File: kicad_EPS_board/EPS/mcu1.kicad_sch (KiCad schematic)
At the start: 37 parts, among them J10 UEXT, P6 CONN_01X02, U10 W25Q80DVS, U11 STM32G431CBTx, Y2 8MHz

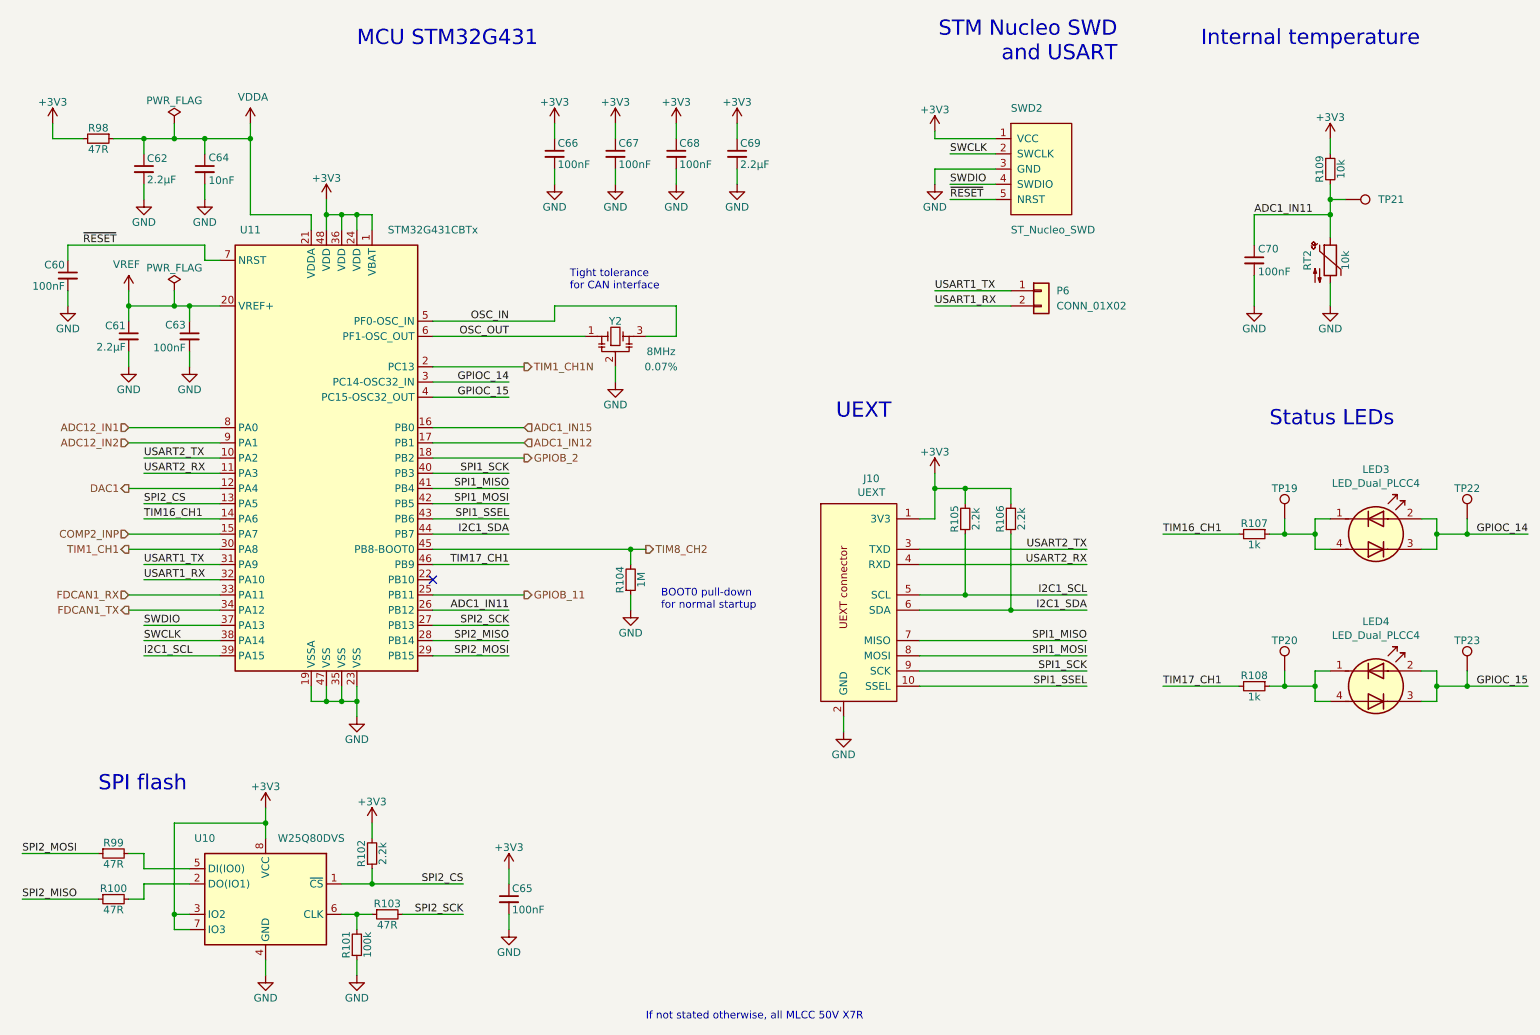
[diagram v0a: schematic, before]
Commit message: kicad EPS board V2 revision and already generated html doc files
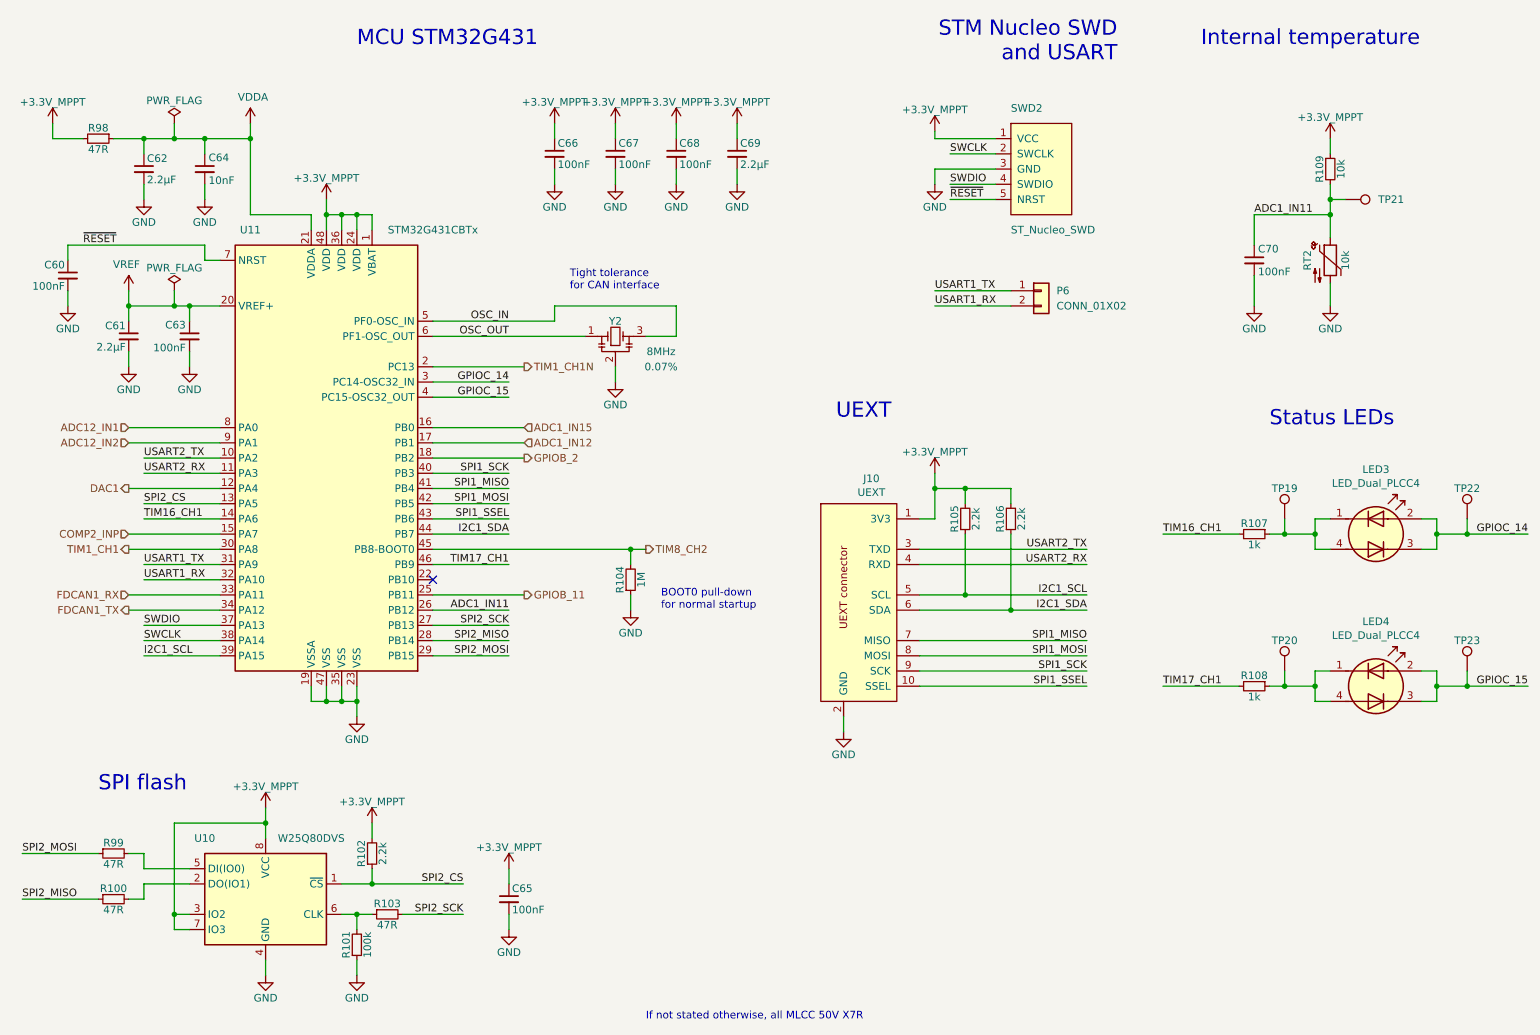
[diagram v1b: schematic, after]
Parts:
- RT2: footprint Capacitor_THT:C_Disc_D3.8mm_W2.6mm_P2.50mm -> Resistor_SMD:R_0603_1608Metric
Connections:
- net +3V3 renamed +3.3V_MPPT
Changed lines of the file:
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@@
 (kicad_sch
-	(version 20231120)
+	(version 20250114)
 	(generator "eeschema")
-	(generator_version "8.0")
+	(generator_version "9.0")
 	(paper "A4")
+	(text "MCU STM32G431"
+		(exclude_from_sim no)
+		(at 83.82 21.59 0)
+		(effects
+			(font
+				(size 2.54 2.54)
+			)
+			(justify left bottom)
+		)
+	)
+	(text "SPI flash"
+		(exclude_from_sim no)
+		(at 40.64 146.05 0)
+		(effects
+			(font
+				(size 2.54 2.54)
+			)
+			(justify left bottom)
+		)
+	)
+	(text "If not stated otherwise, all MLCC 50V X7R"
+		(exclude_from_sim no)
+		(at 132.08 184.15 0)
+		(effects
+			(font
+				(size 1.27 1.27)
+			)
+			(justify left bottom)
+		)
+	)
+	(text "Status LEDs"
+		(exclude_from_sim no)
+		(at 236.22 85.09 0)
+		(effects
+			(font
+				(size 2.54 2.54)
+			)
+			(justify left bottom)
+		)
+	)
+	(text "Internal temperature"
+		(exclude_from_sim no)
+		(at 224.79 21.59 0)
+		(effects
+			(font
+				(size 2.54 2.54)
+			)
+			(justify left bottom)
+		)
+	)
+	(text "Tight tolerance\nfor CAN interface"
+		(exclude_from_sim no)
+		(at 119.38 62.23 0)
+		(effects
+			(font
+				(size 1.27 1.27)
+			)
+			(justify left bottom)
+		)
+	)
+	(text "BOOT0 pull-down\nfor normal startup"
+		(exclude_from_sim no)
+		(at 134.62 115.57 0)
+		(effects
+			(font
+				(size 1.27 1.27)
+			)
+			(justify left bottom)
+		)
+	)
+	(text "UEXT"
+		(exclude_from_sim no)
+		(at 163.83 83.82 0)
+		(effects
+			(font
+				(size 2.54 2.54)
+			)
+			(justify left bottom)
+		)
+	)
+	(text "STM Nucleo SWD\nand USART"
+		(exclude_from_sim no)
+		(at 210.82 24.13 0)
+		(effects
+			(font
+				(size 2.54 2.54)
+			)
+			(justify right bottom)
+		)
+	)
 	(junction
 		(at 246.38 49.53)
@@
 		)
 	)
-	(text "MCU STM32G431"
-		(exclude_from_sim no)
-		(at 83.82 21.59 0)
-		(effects
-			(font
-				(size 2.54 2.54)
-			)
-			(justify left bottom)
-		)
-	)
-	(text "SPI flash"
-		(exclude_from_sim no)
-		(at 40.64 146.05 0)
-		(effects
-			(font
-				(size 2.54 2.54)
-			)
-			(justify left bottom)
-		)
-	)
-	(text "If not stated otherwise, all MLCC 50V X7R"
-		(exclude_from_sim no)
-		(at 132.08 184.15 0)
-		(effects
-			(font
-				(size 1.27 1.27)
-			)
-			(justify left bottom)
-		)
-	)
-	(text "Status LEDs"
-		(exclude_from_sim no)
-		(at 236.22 85.09 0)
-		(effects
-			(font
-				(size 2.54 2.54)
-			)
-			(justify left bottom)
-		)
-	)
-	(text "Internal temperature"
-		(exclude_from_sim no)
-		(at 224.79 21.59 0)
-		(effects
-			(font
-				(size 2.54 2.54)
-			)
-			(justify left bottom)
-		)
-	)
-	(text "Tight tolerance\nfor CAN interface"
-		(exclude_from_sim no)
-		(at 119.38 62.23 0)
-		(effects
-			(font
-				(size 1.27 1.27)
-			)
-			(justify left bottom)
-		)
-	)
-	(text "BOOT0 pull-down\nfor normal startup"
-		(exclude_from_sim no)
-		(at 134.62 115.57 0)
-		(effects
-			(font
-				(size 1.27 1.27)
-			)
-			(justify left bottom)
-		)
-	)
-	(text "UEXT"
-		(exclude_from_sim no)
-		(at 163.83 83.82 0)
-		(effects
-			(font
-				(size 2.54 2.54)
-			)
-			(justify left bottom)
-		)
-	)
-	(text "STM Nucleo SWD\nand USART"
-		(exclude_from_sim no)
-		(at 210.82 24.13 0)
-		(effects
-			(font
-				(size 2.54 2.54)
-			)
-			(justify right bottom)
-		)
-	)
 	(label "SPI1_MOSI"
 		(at 109.22 97.79 180)
@@
 			)
 		)
-		(property "Value" "+3V3"
+		(property "Value" "+3.3V_MPPT"
 			(at 68.58 145.034 0)
 			(effects
@@
 			)
 		)
-		(property "Value" "+3V3"
+		(property "Value" "+3.3V_MPPT"
 			(at 86.36 147.574 0)
 			(effects
@@
 			)
 		)
-		(property "Value" "+3V3"
+		(property "Value" "+3.3V_MPPT"
 			(at 180.34 32.004 0)
 			(effects
@@
 			)
 		)
-		(property "Footprint" "Capacitor_THT:C_Disc_D3.8mm_W2.6mm_P2.50mm"
+		(property "Footprint" "Resistor_SMD:R_0603_1608Metric"
 			(at 246.38 55.88 0)
 			(effects
@@
 			)
 		)
-		(property "Value" "+3V3"
+		(property "Value" "+3.3V_MPPT"
 			(at 137.16 30.734 0)
 			(effects
@@
 			)
 		)
-		(property "Value" "+3V3"
+		(property "Value" "+3.3V_MPPT"
 			(at 78.74 43.434 0)
 			(effects
@@
 			)
 		)
-		(property "Value" "+3V3"
+		(property "Value" "+3.3V_MPPT"
 			(at 246.38 33.274 0)
 			(effects
@@
 			)
 		)
-		(property "Value" "+3V3"
+		(property "Value" "+3.3V_MPPT"
 			(at 127 30.734 0)
 			(effects
@@
 			)
 		)
-		(property "Value" "+3V3"
+		(property "Value" "+3.3V_MPPT"
 			(at 180.34 89.154 0)
 			(effects
@@
 			)
 		)
-		(property "Value" "+3V3"
+		(property "Value" "+3.3V_MPPT"
 			(at 147.32 30.734 0)
 			(effects
@@
 			)
 		)
-		(property "Value" "+3V3"
+		(property "Value" "+3.3V_MPPT"
 			(at 116.84 30.734 0)
 			(effects
@@
 			)
 		)
-		(property "Value" "+3V3"
+		(property "Value" "+3.3V_MPPT"
 			(at 33.02 30.734 0)
 			(effects
@@
 			)
 		)
-		(property "Value" "+3V3"
+		(property "Value" "+3.3V_MPPT"
 			(at 109.22 155.194 0)
 			(effects
